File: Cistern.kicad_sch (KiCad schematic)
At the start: 15 parts, among them J2 Gauge Stepper, J3 Power Connector, Q1 BD244C, SW1 WiFi reset switch, SW2 Water Sensor, U1 ULN2003A, U3 Boost Converter (5->20 V)

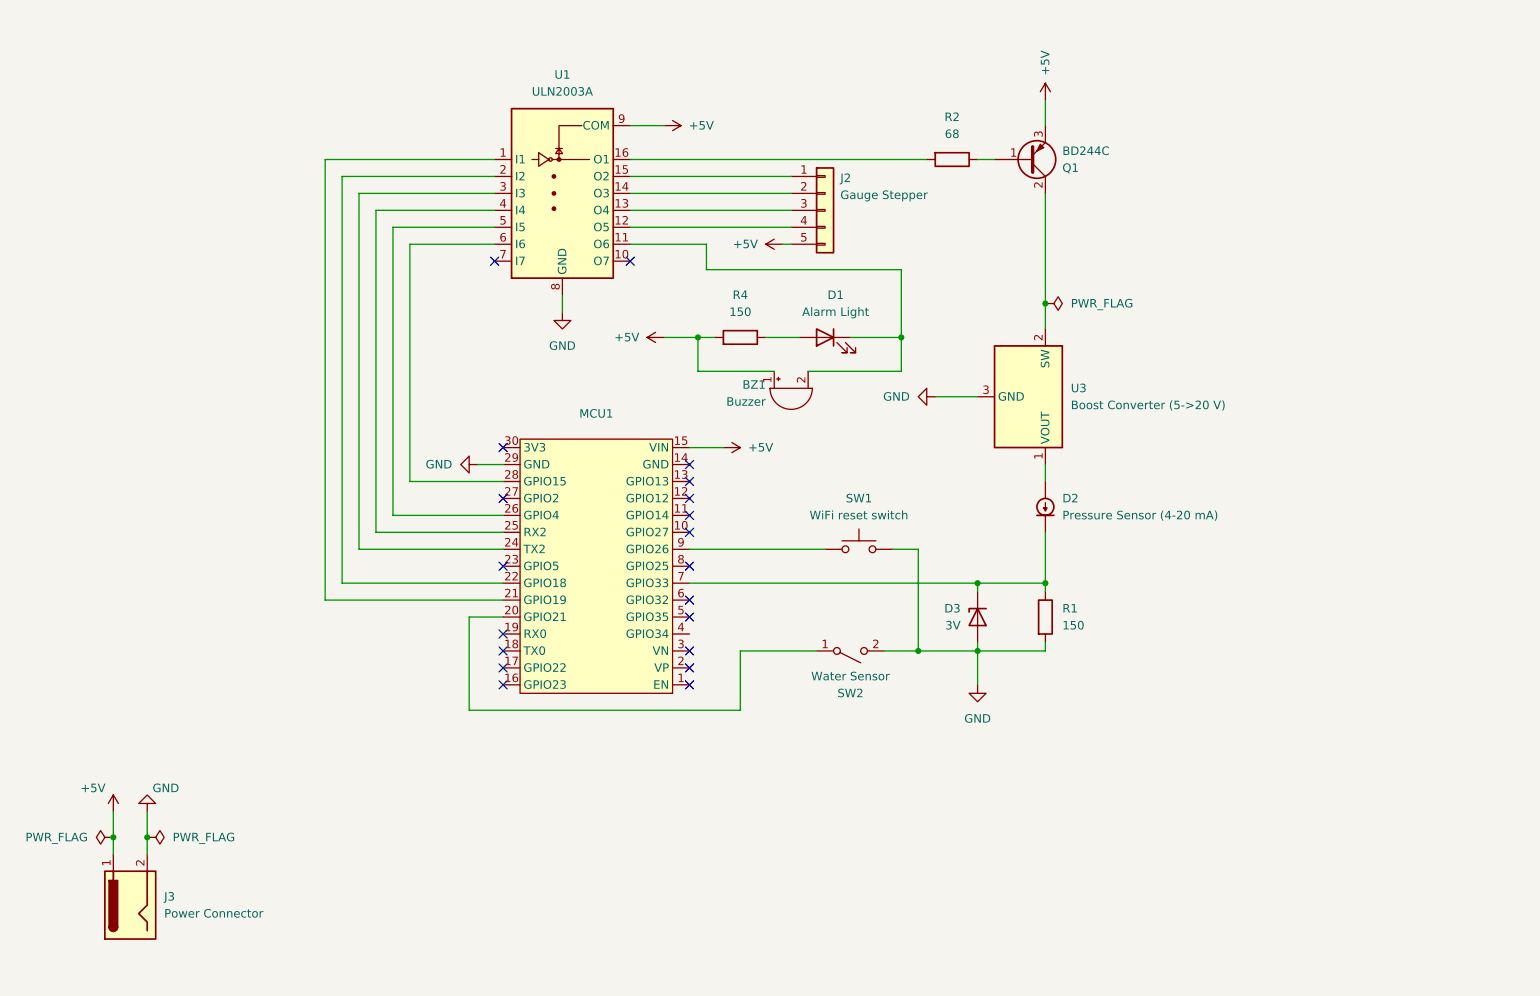
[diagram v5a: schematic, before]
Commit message: Adding gauge calibration sensor
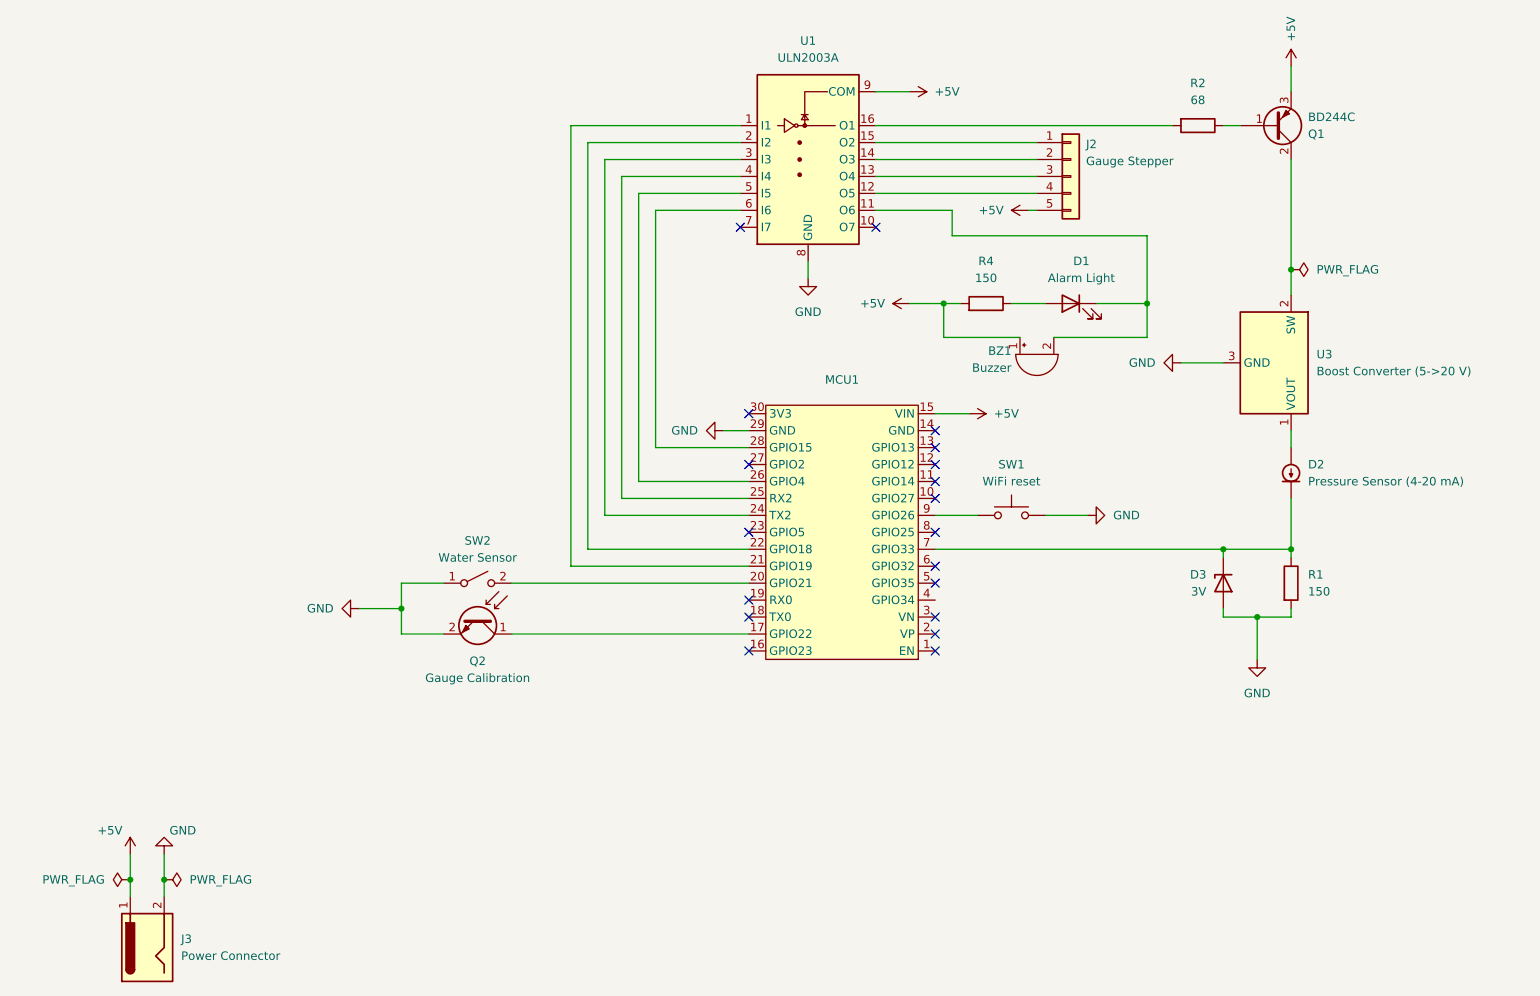
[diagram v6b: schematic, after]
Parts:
- added Q2: Gauge Calibration, Connector_PinHeader_2.54mm:PinHeader_1x02_P2.54mm_Vertical, symbol Device:Q_Photo_NPN
- SW1: value WiFi reset switch -> WiFi reset
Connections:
- net GND: now also SW2.1 (A), Q2.2 (E); no longer SW2.2 (B)
- net at MCU1.17 (GPIO22): now also Q2.1 (C)
- net at MCU1.20 (GPIO21): now also SW2.2 (B); no longer SW2.1 (A)
- no-connect marks 20 -> 19
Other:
- moved on the sheet: BZ1, D1, D2, D3, J2, J3, MCU1, Q1, R1, R2, R4, SW1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

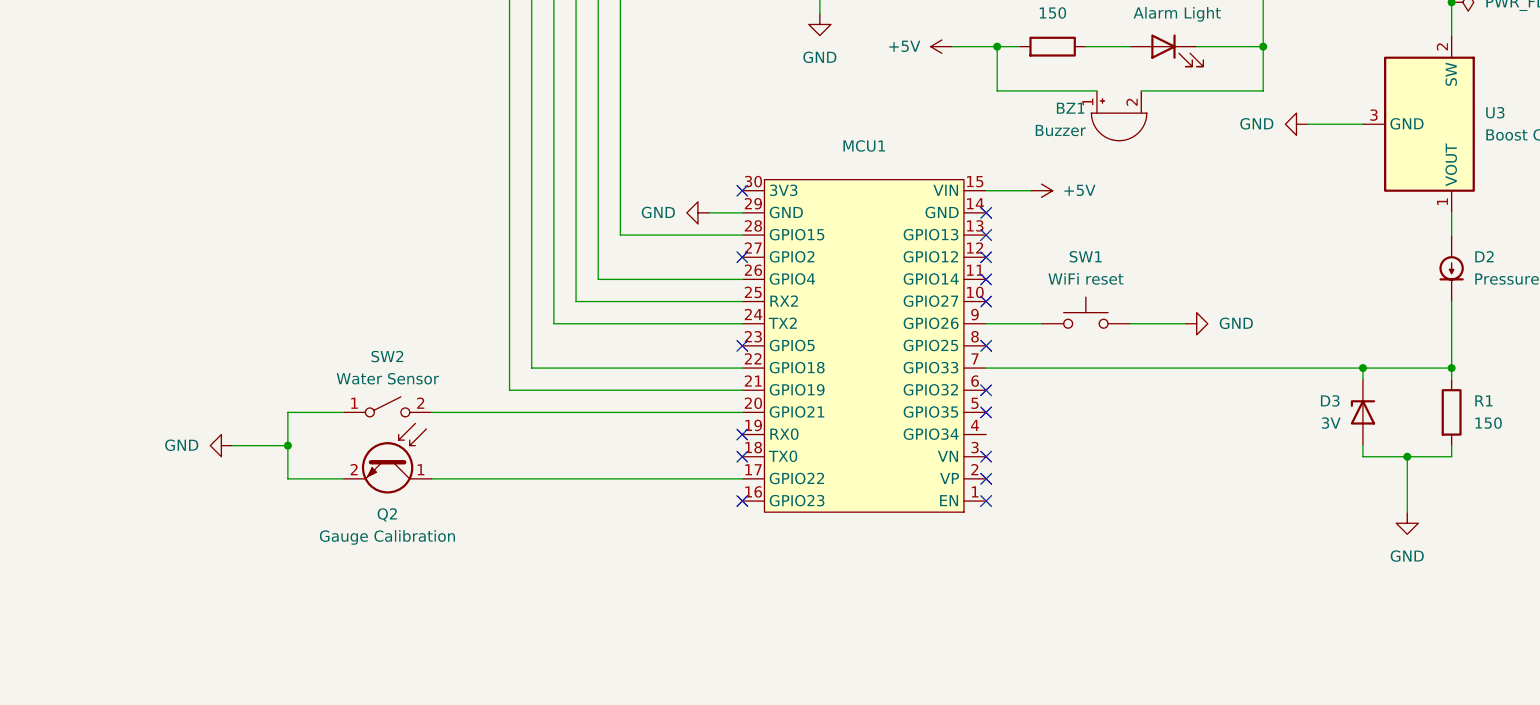
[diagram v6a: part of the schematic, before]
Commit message: Changing pin assignments some more, adding gauge calibration sensor
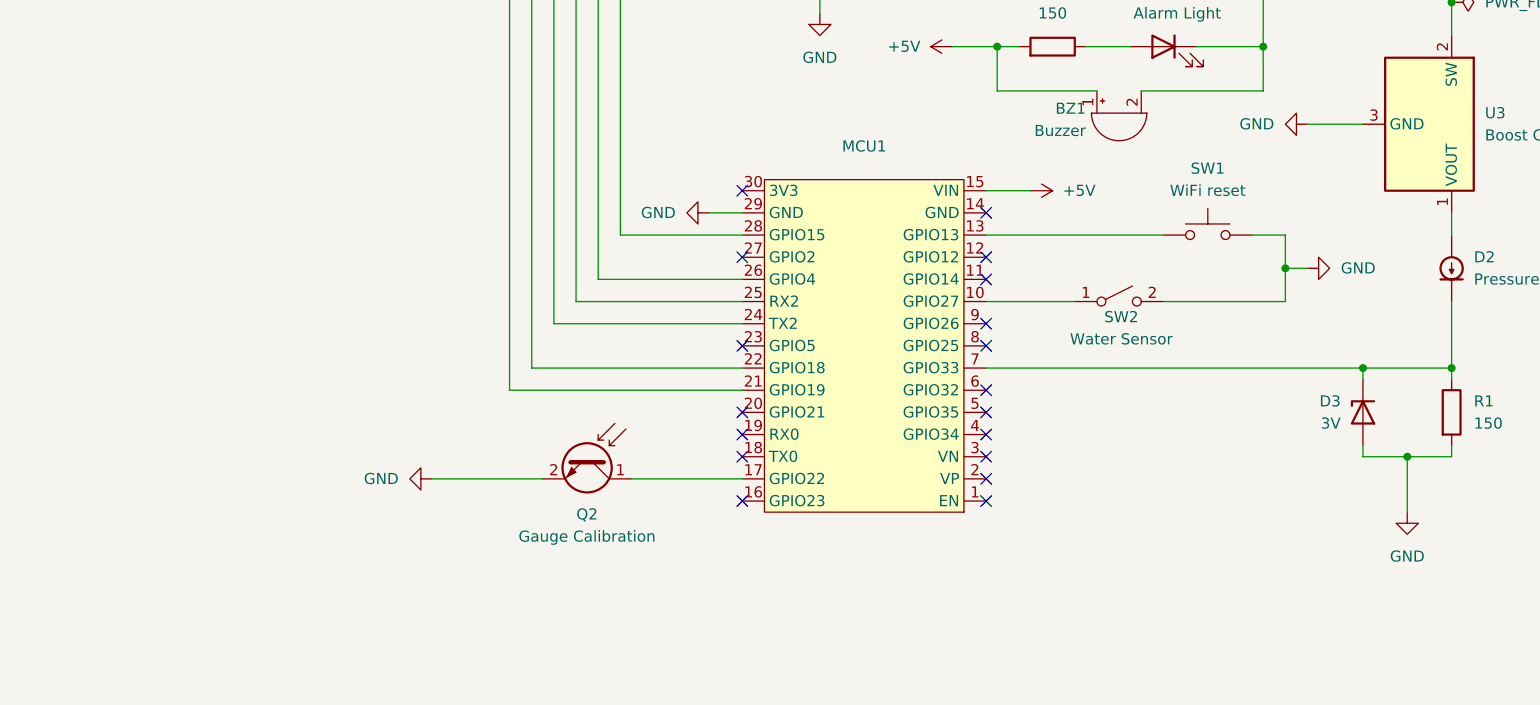
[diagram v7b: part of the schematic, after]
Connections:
- net GND: now also SW2.2 (B); no longer SW2.1 (A)
- net at MCU1.10 (GPIO27): now also SW2.1 (A)
- net at MCU1.13 (GPIO13): now also SW1.1
- net at MCU1.20 (GPIO21): no longer SW2.2 (B)
- net at MCU1.9 (GPIO26): no longer SW1.1
- no-connect marks 19 -> 20
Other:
- moved on the sheet: Q2, SW1, SW2
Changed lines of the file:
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@@
+	)
+	(junction
+		(at 209.55 99.06)
+		(diameter 0)
+		(color 0 0 0 0)
 	)
 	(junction
@@
 	)
 	(junction
-		(at 95.25 119.38)
-		(diameter 0)
-		(color 0 0 0 0)
-	)
-	(junction
 		(at 207.01 73.66)
 		(diameter 0)
@@
 	)
 	(no_connect
+		(at 147.32 115.57)
+	)
+	(no_connect
 		(at 147.32 120.65)
 	)
@@
 	)
 	(no_connect
+		(at 175.26 118.11)
+	)
+	(no_connect
 		(at 175.26 125.73)
-	)
-	(no_connect
-		(at 175.26 95.25)
 	)
 	(no_connect
@@
 	)
 	(no_connect
+		(at 175.26 105.41)
+	)
+	(no_connect
 		(at 175.26 100.33)
-	)
-	(no_connect
-		(at 175.26 102.87)
 	)
 	(no_connect
@@
 	)
 	(no_connect
+		(at 175.26 113.03)
+	)
+	(no_connect
 		(at 175.26 97.79)
-	)
-	(no_connect
-		(at 175.26 113.03)
 	)
 	(no_connect
@@
 	(wire
 		(pts
-			(xy 175.26 105.41) (xy 181.61 105.41)
-		)
-		(stroke
-			(width 0)
-			(type default)
-		)
-	)
-	(wire
-		(pts
 			(xy 120.65 46.99) (xy 120.65 113.03)
 		)
@@
 	(wire
 		(pts
-			(xy 95.25 119.38) (xy 95.25 123.19)
-		)
-		(stroke
-			(width 0)
-			(type default)
-		)
-	)
-	(wire
-		(pts
 			(xy 218.44 110.49) (xy 218.44 111.76)
 		)
@@
 	(wire
 		(pts
-			(xy 191.77 105.41) (xy 198.12 105.41)
+			(xy 205.74 95.25) (xy 209.55 95.25)
 		)
 		(stroke
@@
 	(wire
 		(pts
+			(xy 209.55 99.06) (xy 212.09 99.06)
+		)
+		(stroke
+			(width 0)
+			(type default)
+		)
+	)
+	(wire
+		(pts
 			(xy 223.52 120.65) (xy 228.6 120.65)
 		)
@@
 	(wire
 		(pts
+			(xy 175.26 102.87) (xy 185.42 102.87)
+		)
+		(stroke
+			(width 0)
+			(type default)
+		)
+	)
+	(wire
+		(pts
 			(xy 133.35 59.69) (xy 133.35 95.25)
 		)
@@
 	(wire
 		(pts
-			(xy 88.9 119.38) (xy 95.25 119.38)
+			(xy 111.76 123.19) (xy 124.46 123.19)
 		)
 		(stroke
@@
 	(wire
 		(pts
-			(xy 111.76 115.57) (xy 147.32 115.57)
+			(xy 175.26 95.25) (xy 195.58 95.25)
 		)
 		(stroke
@@
 	(wire
 		(pts
-			(xy 95.25 115.57) (xy 95.25 119.38)
-		)
-		(stroke
-			(width 0)
-			(type default)
-		)
-	)
-	(wire
-		(pts
 			(xy 166.37 54.61) (xy 190.5 54.61)
 		)
@@
 	(wire
 		(pts
+			(xy 209.55 95.25) (xy 209.55 99.06)
+		)
+		(stroke
+			(width 0)
+			(type default)
+		)
+	)
+	(wire
+		(pts
 			(xy 218.44 46.99) (xy 220.98 46.99)
 		)
@@
 	(wire
 		(pts
-			(xy 95.25 123.19) (xy 101.6 123.19)
+			(xy 209.55 99.06) (xy 209.55 102.87)
 		)
 		(stroke
@@
 	(wire
 		(pts
+			(xy 195.58 102.87) (xy 209.55 102.87)
+		)
+		(stroke
+			(width 0)
+			(type default)
+		)
+	)
+	(wire
+		(pts
 			(xy 177.8 63.5) (xy 207.01 63.5)
 		)
@@
 	(wire
 		(pts
-			(xy 101.6 115.57) (xy 95.25 115.57)
-		)
-		(stroke
-			(width 0)
-			(type default)
-		)
-	)
-	(wire
-		(pts
-			(xy 111.76 123.19) (xy 147.32 123.19)
+			(xy 134.62 123.19) (xy 147.32 123.19)
 		)
 		(stroke
@@
 	(symbol
 		(lib_id "power:GND")
-		(at 88.9 119.38 270)
+		(at 111.76 123.19 270)
 		(unit 1)
 		(exclude_from_sim no)
@@
 		(fields_autoplaced yes)
 		(property "Reference" "#PWR09"
-			(at 82.55 119.38 0)
+			(at 105.41 123.19 0)
 			(effects
 				(font
@@
 		)
 		(property "Value" "GND"
-			(at 85.09 119.3799 90)
+			(at 107.95 123.1899 90)
 			(effects
 				(font
@@
 		)
 		(property "Footprint" ""
-			(at 88.9 119.38 0)
+			(at 111.76 123.19 0)
 			(effects
 				(font
@@
 		)
 		(property "Datasheet" ""
-			(at 88.9 119.38 0)
+			(at 111.76 123.19 0)
 			(effects
 				(font
@@
 		)
 		(property "Description" "Power symbol creates a global label with name \"GND\" , ground"
-			(at 88.9 119.38 0)
+			(at 111.76 123.19 0)
 			(effects
 				(font
@@
 	(symbol
 		(lib_id "Switch:SW_SPST")
-		(at 106.68 115.57 0)
+		(at 190.5 102.87 0)
 		(unit 1)
 		(exclude_from_sim no)
@@
 		(dnp no)
 		(property "Reference" "SW2"
-			(at 106.68 109.22 0)
+			(at 190.754 104.648 0)
 			(effects
 				(font
@@
 		)
 		(property "Value" "Water Sensor"
-			(at 106.68 111.76 0)
+			(at 190.754 107.188 0)
 			(effects
 				(font
@@
 		)
 		(property "Footprint" "Connector_PinHeader_2.54mm:PinHeader_1x02_P2.54mm_Vertical"
-			(at 106.68 115.57 0)
+			(at 190.5 102.87 0)
 			(effects
 				(font
@@
 		)
 		(property "Datasheet" "~"
-			(at 106.68 115.57 0)
+			(at 190.5 102.87 0)
 			(effects
 				(font
@@
 		)
 		(property "Description" "Single Pole Single Throw (SPST) switch"
-			(at 106.68 115.57 0)
+			(at 190.5 102.87 0)
 			(effects
 				(font
@@
 	(symbol
 		(lib_id "Device:Q_Photo_NPN")
-		(at 106.68 120.65 270)
+		(at 129.54 120.65 270)
 		(unit 1)
 		(exclude_from_sim no)
@@
 		(dnp no)
 		(property "Reference" "Q2"
-			(at 106.68 127.254 90)
+			(at 129.54 127.254 90)
 			(effects
 				(font
@@
 		)
 		(property "Value" "Gauge Calibration"
-			(at 106.68 129.794 90)
+			(at 129.54 129.794 90)
 			(effects
 				(font
@@
 		)
 		(property "Footprint" "Connector_PinHeader_2.54mm:PinHeader_1x02_P2.54mm_Vertical"
-			(at 109.22 125.73 0)
+			(at 132.08 125.73 0)
 			(effects
 				(font
@@
 		)
 		(property "Datasheet" "~"
-			(at 106.68 120.65 0)
+			(at 129.54 120.65 0)
 			(effects
 				(font
@@
 		)
 		(property "Description" "NPN phototransistor, collector/emitter"
-			(at 106.68 120.65 0)
+			(at 129.54 120.65 0)
 			(effects
 				(font
@@
 	(symbol
 		(lib_id "power:GND")
-		(at 198.12 105.41 90)
+		(at 212.09 99.06 90)
 		(unit 1)
 		(exclude_from_sim no)
@@
 		(fields_autoplaced yes)
 		(property "Reference" "#PWR04"
-			(at 204.47 105.41 0)
+			(at 218.44 99.06 0)
 			(effects
 				(font
@@
 		)
 		(property "Value" "GND"
-			(at 201.93 105.4099 90)
+			(at 215.9 99.0599 90)
 			(effects
 				(font
@@
 		)
 		(property "Footprint" ""
-			(at 198.12 105.41 0)
+			(at 212.09 99.06 0)
 			(effects
 				(font
@@
 		)
 		(property "Datasheet" ""
-			(at 198.12 105.41 0)
+			(at 212.09 99.06 0)
 			(effects
 				(font
@@
 		)
 		(property "Description" "Power symbol creates a global label with name \"GND\" , ground"
-			(at 198.12 105.41 0)
+			(at 212.09 99.06 0)
 			(effects
 				(font
@@
 	(symbol
 		(lib_id "Switch:SW_Push")
-		(at 186.69 105.41 0)
+		(at 200.66 95.25 0)
 		(unit 1)
 		(exclude_from_sim no)
@@
 		(fields_autoplaced yes)
 		(property "Reference" "SW1"
-			(at 186.69 97.79 0)
+			(at 200.66 87.63 0)
 			(effects
 				(font
@@
 		)
 		(property "Value" "WiFi reset"
-			(at 186.69 100.33 0)
+			(at 200.66 90.17 0)
 			(effects
 				(font
@@
 		)
 		(property "Footprint" "Button_Switch_THT:SW_PUSH_6mm"
-			(at 186.69 100.33 0)
+			(at 200.66 90.17 0)
 			(effects
 				(font
@@
 		)
 		(property "Datasheet" "~"
-			(at 186.69 100.33 0)
+			(at 200.66 90.17 0)
 			(effects
 				(font
@@
 		)
 		(property "Description" "Push button switch, generic, two pins"
-			(at 186.69 105.41 0)
-			(effects
-				(font
+			(at 200.66 95.25 0)
+			(effects
+				(font

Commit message: Finishing first version of board layout
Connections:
- net GND: now also MCU1.14 (GND)
- no-connect marks 20 -> 19
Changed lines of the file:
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@@
-	)
-	(no_connect
-		(at 175.26 92.71)
 	)
 	(no_connect
@@
 		(pts
 			(xy 180.34 90.17) (xy 175.26 90.17)
+		)
+		(stroke
+			(width 0)
+			(type default)
+		)
+	)
+	(wire
+		(pts
+			(xy 175.26 92.71) (xy 180.34 92.71)
 		)
 		(stroke
@@
 					(unit 1)
 				)
+			)
+		)
+	)
+	(symbol
+		(lib_id "power:GND")
+		(at 180.34 92.71 90)
+		(unit 1)
+		(exclude_from_sim no)
+		(in_bom yes)
+		(on_board yes)
+		(dnp no)
+		(fields_autoplaced yes)
+		(property "Reference" "#PWR014"
+			(at 186.69 92.71 0)
+			(effects
+				(font
+					(size 1.27 1.27)
+				)
+				(hide yes)
+			)
+		)
+		(property "Value" "GND"
+			(at 184.15 92.7099 90)
+			(effects
+				(font
+					(size 1.27 1.27)
+				)
+				(justify right)
+			)
+		)
+		(property "Footprint" ""
+			(at 180.34 92.71 0)
+			(effects
+				(font
+					(size 1.27 1.27)
+				)
+				(hide yes)
+			)
+		)
+		(property "Datasheet" ""
+			(at 180.34 92.71 0)
+			(effects
+				(font
+					(size 1.27 1.27)
+				)
+				(hide yes)
+			)
+		)
+		(property "Description" "Power symbol creates a global label with name \"GND\" , ground"
+			(at 180.34 92.71 0)
+			(effects
+				(font
+					(size 1.27 1.27)
+				)
+				(hide yes)
+			)
+		)
+		(pin "1"
+		)
+		(instances
+			(project "Cistern"
+				(path "/387a1b1b-4d04-4a4f-a341-bb26b6058549"
+					(reference "#PWR014")
+					(unit 1)
+				)
